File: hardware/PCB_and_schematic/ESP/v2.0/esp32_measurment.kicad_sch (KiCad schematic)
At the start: 73 parts, among them J1 OR-OR SMOKE SENSOR, J10 CO_SENSOR, J11 H2_SENSOR, J2 LCD_DISP, J4 RS485, J5 DHT22, J6 DC_LINE_OUTPUT, J9 DB9_Socket, Q1 BC817, Q11 BC817, Q2 BC817, Q3 BC817, Q6 BSS138, Q7 BSS138, Q8 BC817, SW1 SW_Push, U1 PCF8574, U2 ST485, U3 AMS1117-5.0, U5 ESP32_DevKit_V1_DOIT, U7 MAX3232, U9 UP7760

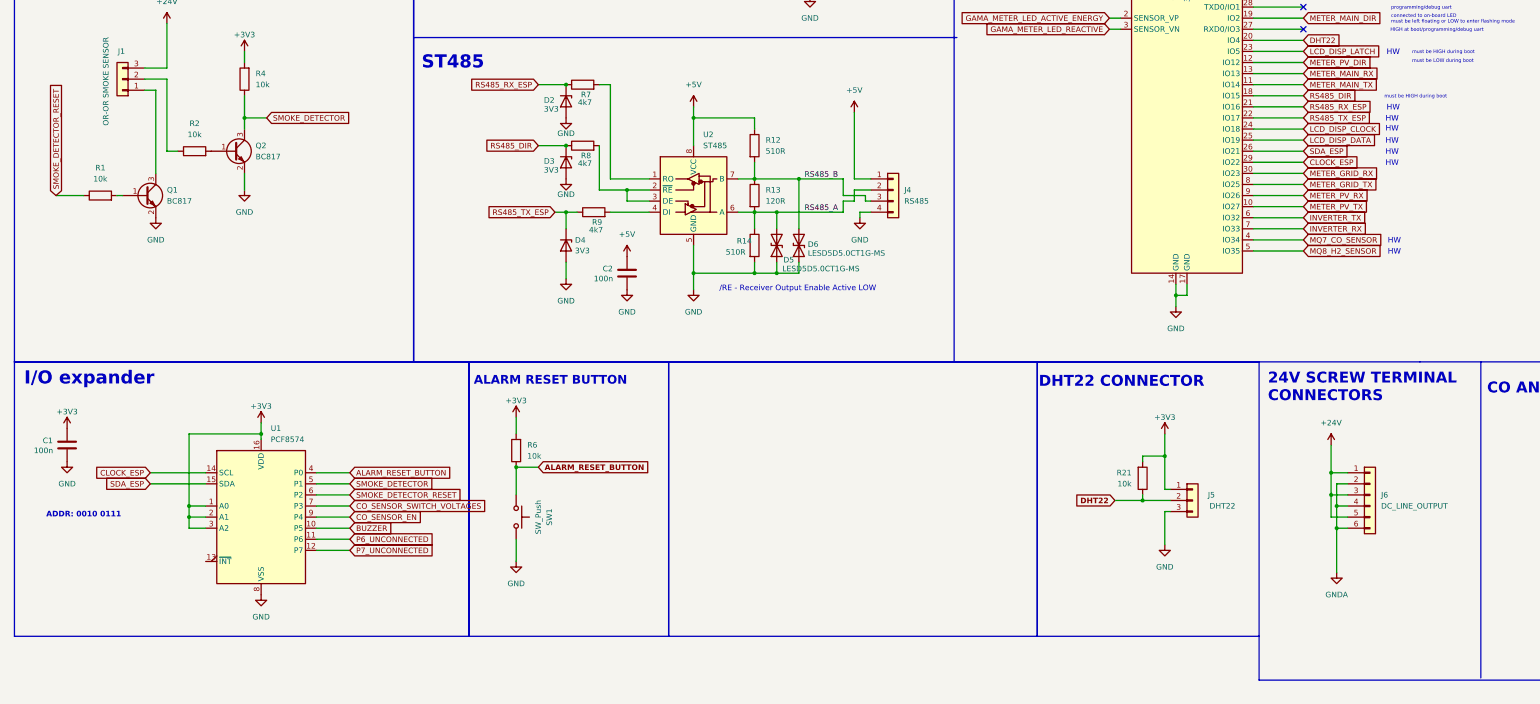
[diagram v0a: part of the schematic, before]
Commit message: esp32 schematic update
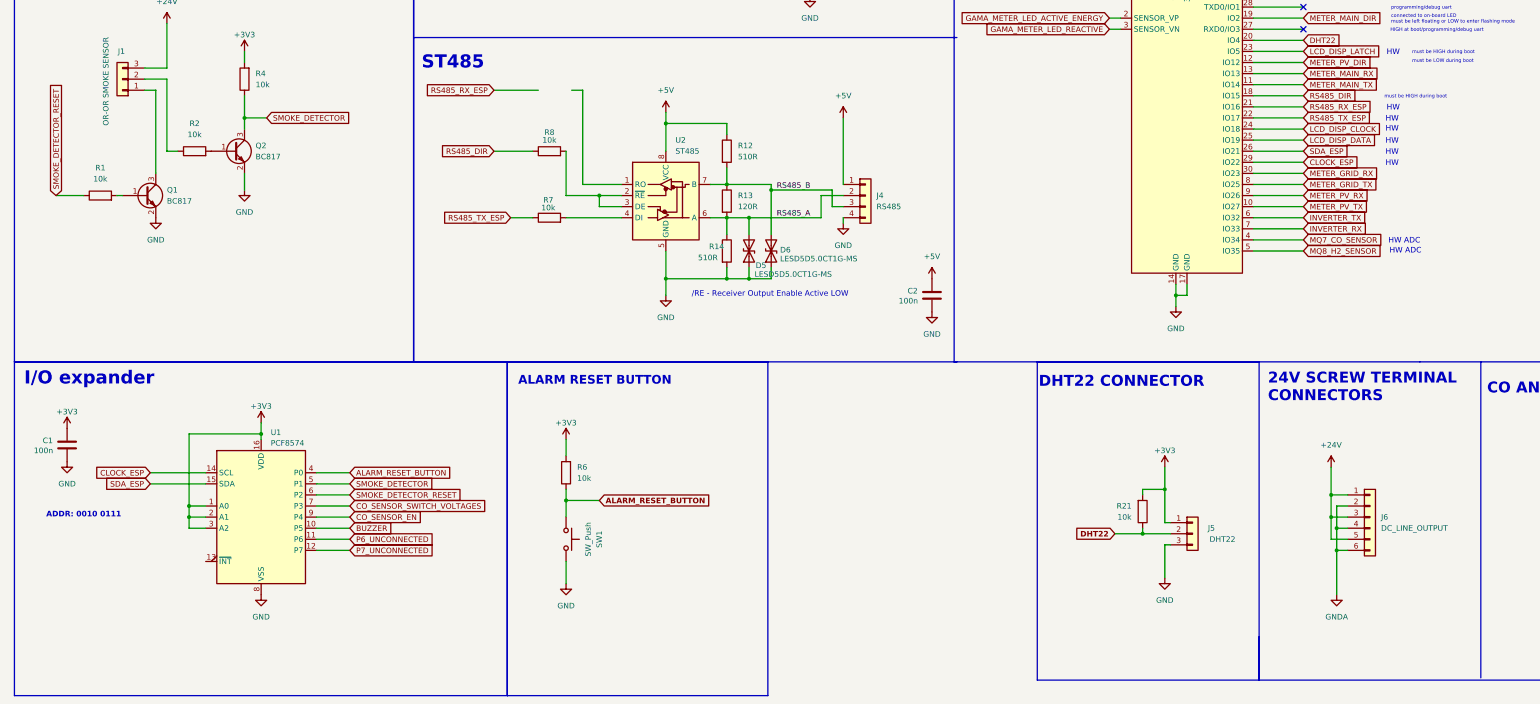
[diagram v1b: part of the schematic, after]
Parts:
- removed D2, D3, D4: 3V3, Diode_SMD:D_MiniMELF, symbol Device:D_Zener
- removed R9: 4k7, Resistor_SMD:R_0805_2012Metric_Pad1.20x1.40mm_HandSolder, symbol Device:R
- R7, R8: value 4k7 -> 10k
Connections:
- net RS485_RX_ESP: no longer R7.1
- net RS485_TX_ESP: now also R7.1
- net at U2.4 (DI): now also R7.2
- net at U2.1 (RO): no longer R7.2
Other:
- note added: "HW ADC"
- moved on the sheet: C2, D5, D6, J4, J5, J6, R12, R13, R14, R21, R6, SW1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

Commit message: add esp32 pcb connectors and logic translators
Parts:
- added D2, D3, D4: BZV55B3V6, Diode_SMD:D_MiniMELF, symbol Diode:BZV55B3V6
- added J10: Unconnected, My-Footprints-connectors:PinHeader_1x04_P2.54mm_thicker, symbol Connector_Generic:Conn_01x04
- added R10: 10k, Resistor_SMD:R_0805_2012Metric_Pad1.20x1.40mm_HandSolder, symbol Device:R
- added R14, R18: 0R, Resistor_SMD:R_0805_2012Metric_Pad1.20x1.40mm_HandSolder, symbol Device:R
- added R9: 4k7/5k1, Resistor_SMD:R_0805_2012Metric_Pad1.20x1.40mm_HandSolder, symbol Device:R
- R6: renamed from R8; value 10k -> 4k7
- R7: value 10k -> 4k7
- renumbered C14 to C10, C16 to C11, C17 to C12, C18 to C13, C19 to C14, C20 to C15, C3 to C2, C4 to C3, C6 to C4, C8 to C5, C2 to C6, C9 to C7, C11 to C8, C12 to C9, F2 to F1, J4 to J3, J5 to J4, J6 to J5, J9 to J6, J10 to J7, J11 to J8, MOD2 to MOD1, Q8 to Q4, Q11 to Q5, R12 to R11, R13 to R12, R14 to R13, R41 to R15, R18 to R16, R21 to R17, R48 to R19, R29 to R20, R30 to R21, R28 to R22, R32 to R23, R35 to R24, R31 to R25, R38 to R26, R39 to R27, R40 to R28, R46 to R29, R47 to R30, R6 to R8, U5 to U4, U9 to U5, U7 to U6
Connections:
- net +3V3: now also J10.1 (Pin_1)
- net GND: now also D2.2 (A), D3.2 (A), D4.2 (A), J10.4 (Pin_4), R10.1
- net P6_UNCONNECTED: now also J10.2 (Pin_2), R14.2
- net P6_UNCONNECTED_OUTPUT: now also R14.1
- net P7_UNCONNECTED: now also J10.3 (Pin_3), R18.2
- net P7_UNCONNECTED_OUTPUT: now also R18.1
- net RS485_DIR: now also D2.1 (K)
- net RS485_RX_ESP: now also R9.1
- net RS485_TX_ESP: now also D3.1 (K)
- net at U2.1 (RO): now also D4.1 (K), R10.2, R9.2
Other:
- moved on the sheet: D5, D6, J3, Q4, Q5, R11, R12, R13, R15, R19, R6, R7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

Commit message: esp32 master update
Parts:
- removed D2, D3, D4: BZV55B3V6, Diode_SMD:D_MiniMELF, symbol Diode:BZV55B3V6
- removed R10: 10k, Resistor_SMD:R_0805_2012Metric_Pad1.20x1.40mm_HandSolder, symbol Device:R
- removed R6, R7: 4k7, Resistor_SMD:R_0805_2012Metric_Pad1.20x1.40mm_HandSolder, symbol Device:R
- removed R9: 4k7/5k1, Resistor_SMD:R_0805_2012Metric_Pad1.20x1.40mm_HandSolder, symbol Device:R
- added C21, C23, C27, C29: 10u, Capacitor_SMD:C_1206_3216Metric, symbol Device:C
- added C22, C24, C26, C28, C30, C31, C32: 100n, Capacitor_SMD:C_0805_2012Metric_Pad1.18x1.45mm_HandSolder, symbol Device:C
- added H1, H2, H3, H4: MountingHole, My-Footprints:Mount-Hole-3mm, symbol Mechanical:MountingHole
- added Q8: BC817, Package_TO_SOT_SMD:SOT-23, symbol Transistor_BJT:BC817
- added R56, R57: 1k, Resistor_SMD:R_0805_2012Metric_Pad1.20x1.40mm_HandSolder, symbol Device:R
- added R58: 4k7, Resistor_SMD:R_0805_2012Metric_Pad1.20x1.40mm_HandSolder, symbol Device:R
- added U10, U13: ADUM3211ARZ, Package_SO:SO-8_3.9x4.9mm_P1.27mm, symbol My-Lib:ADUM3211ARZ
- added U11: PC817, Package_DIP:DIP-4_W7.62mm, symbol Isolator:PC817
- added U12, U15: B0505S-1W, My-Footprints:B0505S, symbol My-Lib:B0505S-1W
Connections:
- net +3V3: now also U10.1 (VDD1), U11.1, U13.1 (VDD1); no longer C10.1, C11.2, C9.2, U6.16 (VCC)
- net +5V: now also C21.1, C22.1, C27.1, C28.1, U12.1 (GND), U15.1 (GND); no longer C6.1, J3.1 (Pin_1), R11.1, U2.8 (VCC)
- net GND: now also C21.2, C22.2, C27.2, C28.2, Q8.2 (E), U10.4 (GND1), U12.2 (VIN), U13.4 (GND1), U15.2 (VIN); no longer C12.1, C6.2, D5.1 (A1), D6.1 (A1), J3.4 (Pin_4), J6.5, R13.2, R22.2, R25.1, U2.5 (GND), U6.15 (GND)
- net INVERTER_RX: now also U13.2 (VOA); no longer U6.10 (T2IN)
- net INVERTER_TX: now also U13.3 (VIB); no longer U6.9 (R2OUT)
- net RS485_DIR: now also R56.1
- net RS485_RX_ESP: now also U10.2 (VOA)
- net RS485_TX_ESP: now also U10.3 (VIB)
- net at U2.2 (~{RE}), U2.3 (DE): now also R58.2, U11.4
- net at U2.1 (RO): now also U10.7 (VIA)
- net at U2.4 (DI): now also U10.6 (VOB)
- new net: U13.6 (VOB), U6.10 (T2IN)
- new net: U13.7 (VIA), U6.9 (R2OUT)
- new net: R57.2, U11.2
- new net: Q8.3 (C), R57.1
- new net: Q8.1 (B), R56.2
- new net +5V_INV: C10.1, C11.2, C29.1, C30.1, C31.1, C32.1, C9.2, U13.8 (VDD2), U15.4 (VOUT), U6.16 (VCC)
- new net +5V_RS485: C23.1, C24.1, C26.1, C6.1, J3.1 (Pin_1), R11.1, R58.1, U10.8 (VDD2), U12.4 (VOUT), U2.8 (VCC)
- new net GND_INV: C12.1, C29.2, C30.2, C31.2, C32.2, J6.5, R22.2, R25.1, U13.5 (GND2), U15.3 (0V), U6.15 (GND)
- new net GND_RS485: C23.2, C24.2, C26.2, C6.2, D5.1 (A1), D6.1 (A1), J3.4 (Pin_4), R13.2, U10.5 (GND2), U11.3, U12.3 (0V), U2.5 (GND)
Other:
- note removed: "ST485"
- moved on the sheet: C10, C11, C12, C13, C2, C3, C4, C5, C8, C9, F1, J6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

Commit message: esp master v2.0 routing progress
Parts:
- removed C11, C12, C13, C8: 10u, Capacitor_THT:CP_Radial_D5.0mm_P2.00mm, symbol Device:C_Polarized
- removed C31: 100n, Capacitor_SMD:C_0805_2012Metric_Pad1.18x1.45mm_HandSolder, symbol Device:C
- added C11, C12, C13, C8: 100n, Capacitor_SMD:C_0805_2012Metric_Pad1.18x1.45mm_HandSolder, symbol Device:C
- added F2: Polyfuse, Fuse:Fuse_2920_7451Metric, symbol Device:Polyfuse
- added J9: Unconnected, Connector_JST:JST_XA_B04B-XASK-1_1x04_P2.50mm_Vertical, symbol Connector_Generic:Conn_01x04
- added R6, R7: 0R, Resistor_SMD:R_0805_2012Metric_Pad1.20x1.40mm_HandSolder, symbol Device:R
- added U9: 74HC14, Package_SO:SOIC-14_3.9x8.7mm_P1.27mm, symbol 74xx:74HC14
- J1: footprint Connector_JST:JST_XH_B3B-XH-A_1x03_P2.50mm_Vertical -> Connector_JST:JST_XA_B03B-XASK-1_1x03_P2.50mm_Vertical
- J10: footprint My-Footprints-connectors:PinHeader_1x04_P2.54mm_thicker -> Connector_JST:JST_XA_B04B-XASK-1_1x04_P2.50mm_Vertical
- J2: footprint Connector_JST:JST_EH_B5B-EH-A_1x05_P2.50mm_Vertical -> Connector_JST:JST_XA_B05B-XASK-1_1x05_P2.50mm_Vertical
- J4: footprint Connector_PinHeader_2.54mm:PinHeader_1x03_P2.54mm_Vertical -> My-Footprints-connectors:JST_XA_1x03_P2.54mm_Vertical
- J7, J8: footprint Connector_PinHeader_2.54mm:PinHeader_1x03_P2.54mm_Vertical -> Connector_JST:JST_XA_B03B-XASK-1_1x03_P2.50mm_Vertical
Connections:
- net +24V: now also F2.1; no longer J5.1 (Pin_1), J5.3 (Pin_3), J5.5 (Pin_5)
- net +5V: now also J10.2 (Pin_2)
- net +5V_INV: now also C11.1
- net GND: now also J10.3 (Pin_3); no longer C10.2, C9.1
- net GND_INV: now also C10.2, C9.1, C12.2
- net P6_UNCONNECTED: now also R6.1; no longer J10.2 (Pin_2)
- net P7_UNCONNECTED: now also R7.1; no longer J10.3 (Pin_3)
- net at U6.2 (VS+): now also C11.2
- net at U6.4 (C2+): now also C8.1
- net at U6.5 (C2-): now also C8.2
- net at U6.6 (VS-): now also C12.1
- net at U6.1 (C1+): now also C13.1
- net at U6.3 (C1-): now also C13.2
- net P6_UNCONNECTED_OUTPUT: no longer names the net of Q4.3 (C), R14.1
- net P6_UNCONNECTED_OUTPUT: now also J9.3 (Pin_3)
- net P7_UNCONNECTED_OUTPUT: no longer names the net of Q5.3 (C), R18.1
- net P7_UNCONNECTED_OUTPUT: now also J9.4 (Pin_4)
- new net: R6.2, U9.10
- new net: J9.1 (Pin_1), U9.11
- new net: F2.2, J5.1 (Pin_1), J5.3 (Pin_3), J5.5 (Pin_5)
- new net: R7.2, U9.12
- new net: J9.2 (Pin_2), U9.13
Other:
- moved on the sheet: C32, J10, Q4, Q5, R14, R15, R18, R19

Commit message: done routing esp32 master
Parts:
- added R10, R9: 10k, Resistor_SMD:R_0805_2012Metric_Pad1.20x1.40mm_HandSolder, symbol Device:R
- R11, R13: value 510R -> 1k
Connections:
- net 24V_MEASURED is gone; now on net +24V: MOD1.2 (IN+)
- net GNDA is gone; now on net GND: J5.2 (Pin_2), J5.4 (Pin_4), J5.6 (Pin_6)
- net +3V3: now also R10.2, R9.2
- net CLOCK_ESP: now also R10.1
- net SDA_ESP: now also R9.1
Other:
- note added: "SPRARE I/O PINS USAGE: - NORMAL I/O SOLDER R14, R19, REMOVE R6,R7 - OPEN COLLECTOR: SOLDER Q4, Q5, R15, R19, REMOVE: R14,R48,R6,R7 - SCHMITT GATE INPUT: REMOVE, R14,R15,Q4,R18,R19,Q5"
- moved on the sheet: C1, C10, C11, C12, C13, C21, C22, C23, C24, C26, C27, C28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
